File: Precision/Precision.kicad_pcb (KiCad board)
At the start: 2 copper layers, 152 parts, among them J1 M04PTH, J2 M04PTH, J3 M06SIP, J4 M04PTH, J405 Conn_01x08, J406 Conn_01x08, J5 M06SIP, J6 M02PTH, U401 ATMEGA328P-AU, U501 FT232RL, U602 ZF7, Y401 16MHz

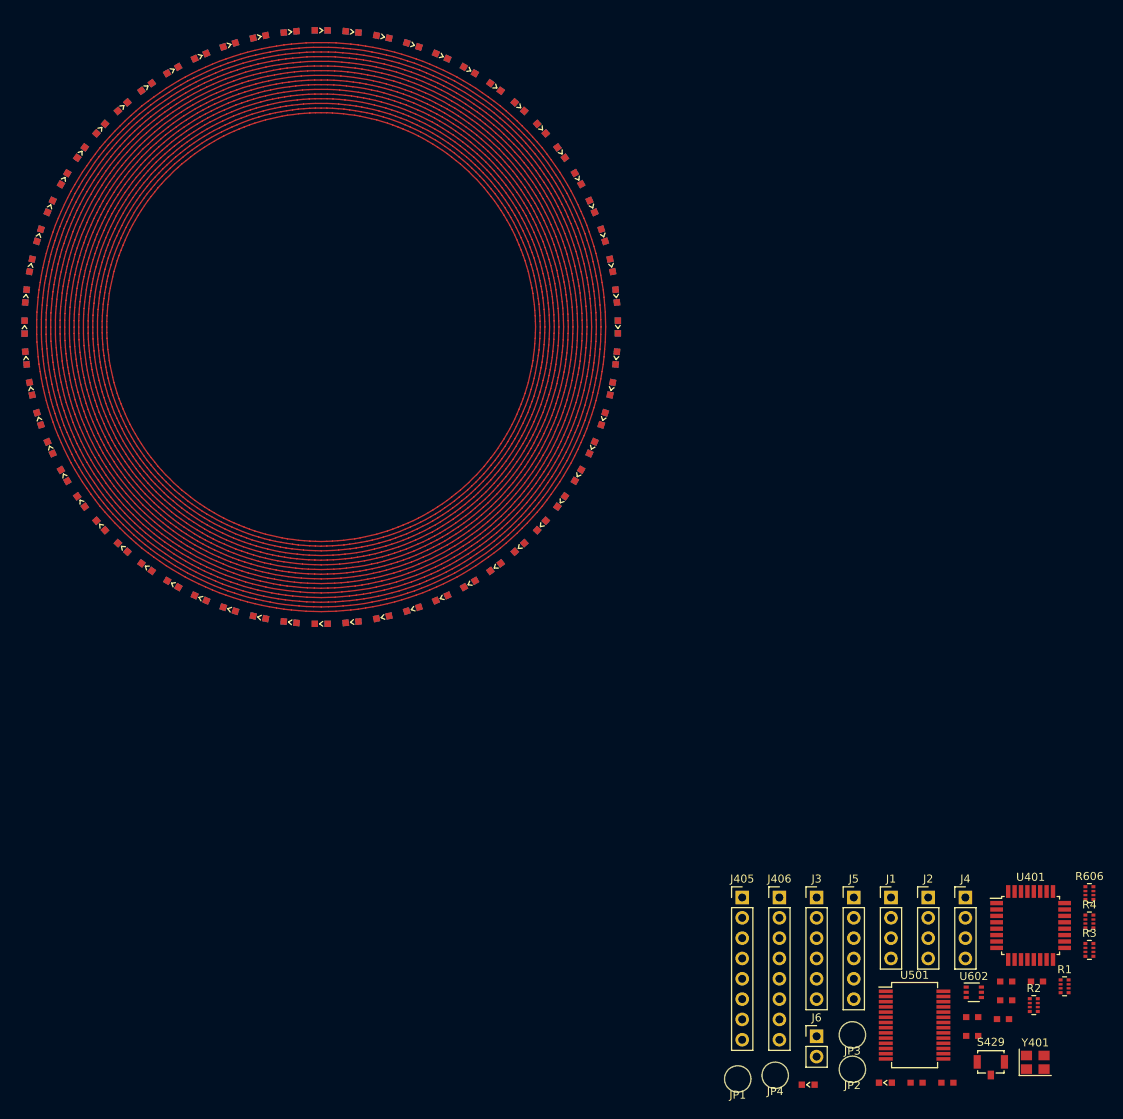
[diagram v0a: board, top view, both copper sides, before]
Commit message: Added Charlieplex traces. The bulk was done with CharlieplexTraces.py, with quite a bit of hand-optimization afterwards
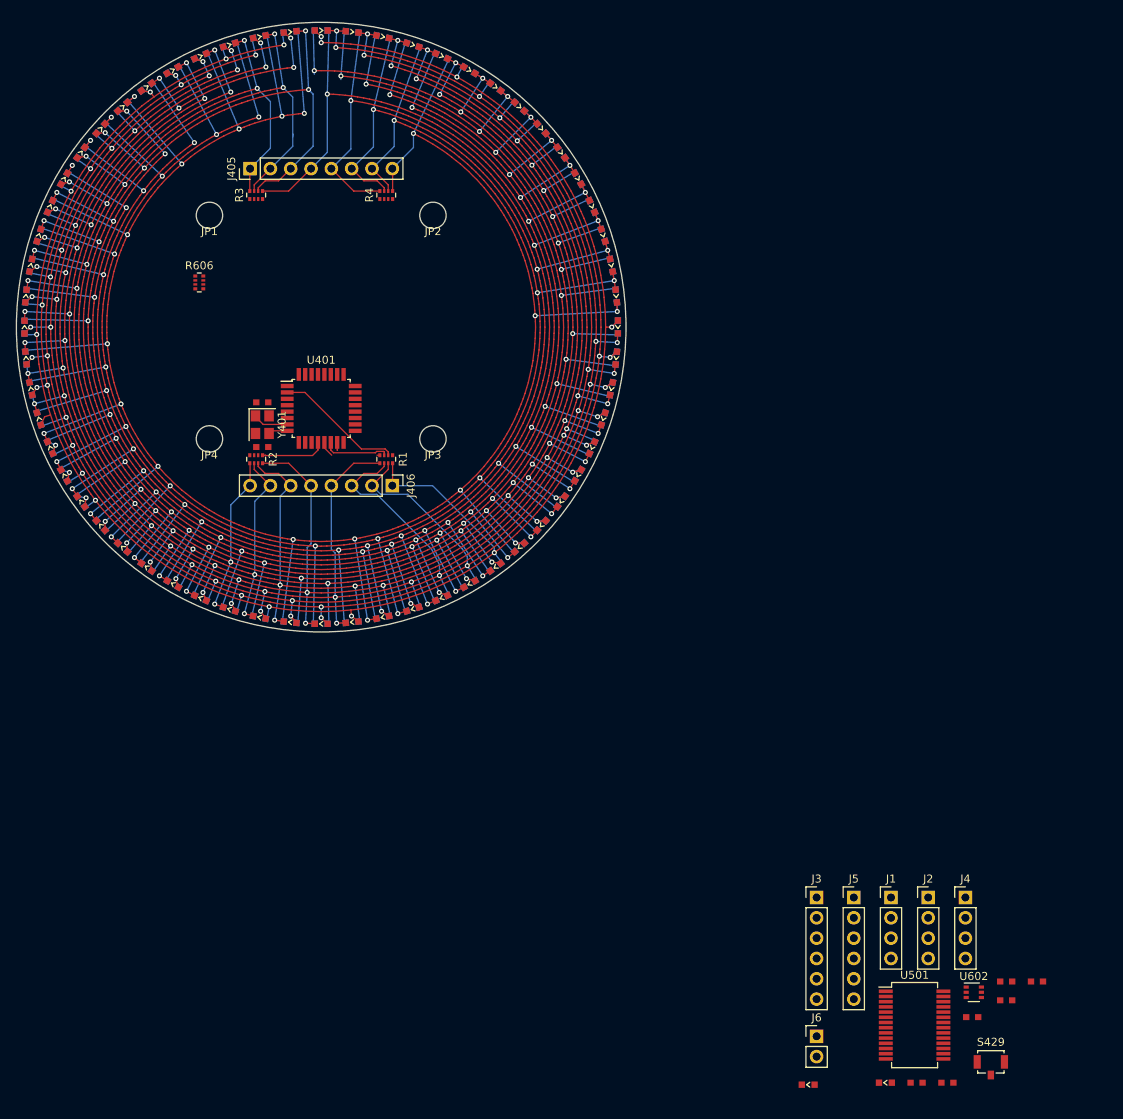
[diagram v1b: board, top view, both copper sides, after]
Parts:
- moved R3 140.5 mm to (42.7, 34.3), turned to 90 degrees
- moved R606 134.9 mm to (35.6, 45.2)
- moved JP1 126.5 mm to (36.8, 36.8)
- moved R4 126.4 mm to (58.9, 34.3), turned to 90 degrees
- moved Y401 125.3 mm to (43.4, 63.0), turned to 270 degrees
- moved C407 120.5 mm to (43.4, 60.2), turned to 180 degrees
- moved JP2 118.9 mm to (64.8, 36.8)
- moved R2 118.8 mm to (42.7, 67.3), turned to 270 degrees
- moved C408 115.3 mm to (43.4, 65.8)
- moved J405 109.9 mm to (41.9, 31.0), turned to 90 degrees
- moved U401 109.7 mm to (50.8, 61.0)
- moved R1 107.4 mm to (58.9, 67.3), turned to 270 degrees
- moved JP4 106.4 mm to (36.8, 64.8)
- moved JP3 91.1 mm to (64.8, 64.8)
- moved J406 70.7 mm to (59.7, 70.6), turned to 270 degrees
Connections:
- D000 pad 1: /Q01 -> /Q02
- D000 pad 2: /Q02 -> /Q01
- D001 pad 1: /Q02 -> /Q03
- D001 pad 2: /Q03 -> /Q02
- D002 pad 1: /Q03 -> /Q04
- D002 pad 2: /Q04 -> /Q03
- D003 pad 1: /Q04 -> /Q05
- D003 pad 2: /Q05 -> /Q04
- D004 pad 1: /Q05 -> /Q06
- D004 pad 2: /Q06 -> /Q05
- D005 pad 1: /Q06 -> /Q07
- D005 pad 2: /Q07 -> /Q06
- D006 pad 1: /Q07 -> /Q08
- D006 pad 2: /Q08 -> /Q07
- D007 pad 1: /Q08 -> /Q09
- D007 pad 2: /Q09 -> /Q08
- D008 pad 1: /Q09 -> /Q10
- D008 pad 2: /Q10 -> /Q09
- D009 pad 1: /Q10 -> /Q11
- D009 pad 2: /Q11 -> /Q10
- D010 pad 1: /Q11 -> /Q12
- D010 pad 2: /Q12 -> /Q11
- D011 pad 1: /Q12 -> /Q13
- D011 pad 2: /Q13 -> /Q12
- D012 pad 1: /Q13 -> /Q14
- D012 pad 2: /Q14 -> /Q13
- D013 pad 1: /Q14 -> /Q15
- D013 pad 2: /Q15 -> /Q14
- D014 pad 1: /Q15 -> /Q16
- D014 pad 2: /Q16 -> /Q15
- D015 pad 1: /Q01 -> /Q03
- D015 pad 2: /Q03 -> /Q01
- D016 pad 1: /Q02 -> /Q04
- D016 pad 2: /Q04 -> /Q02
- D017 pad 1: /Q03 -> /Q05
- D017 pad 2: /Q05 -> /Q03
- D018 pad 1: /Q04 -> /Q06
- D018 pad 2: /Q06 -> /Q04
- D019 pad 1: /Q05 -> /Q07
- D019 pad 2: /Q07 -> /Q05
- D020 pad 1: /Q06 -> /Q08
- D020 pad 2: /Q08 -> /Q06
- D021 pad 1: /Q07 -> /Q09
- D021 pad 2: /Q09 -> /Q07
- D022 pad 1: /Q08 -> /Q10
- D022 pad 2: /Q10 -> /Q08
- D023 pad 1: /Q09 -> /Q11
- D023 pad 2: /Q11 -> /Q09
- D024 pad 1: /Q10 -> /Q12
- D024 pad 2: /Q12 -> /Q10
- D025 pad 1: /Q11 -> /Q13
- D025 pad 2: /Q13 -> /Q11
- D026 pad 1: /Q12 -> /Q14
- D026 pad 2: /Q14 -> /Q12
- D027 pad 1: /Q13 -> /Q15
- D027 pad 2: /Q15 -> /Q13
- D028 pad 1: /Q14 -> /Q16
- D028 pad 2: /Q16 -> /Q14
- D029 pad 1: /Q01 -> /Q04
- D029 pad 2: /Q04 -> /Q01
- D030 pad 1: /Q02 -> /Q05
- D030 pad 2: /Q05 -> /Q02
- D031 pad 1: /Q03 -> /Q06
- D031 pad 2: /Q06 -> /Q03
- D032 pad 1: /Q04 -> /Q07
- D032 pad 2: /Q07 -> /Q04
- D033 pad 1: /Q05 -> /Q08
- D033 pad 2: /Q08 -> /Q05
- D034 pad 1: /Q06 -> /Q09
- D034 pad 2: /Q09 -> /Q06
- D035 pad 1: /Q07 -> /Q10
- D035 pad 2: /Q10 -> /Q07
- D036 pad 1: /Q08 -> /Q11
- D036 pad 2: /Q11 -> /Q08
- D037 pad 1: /Q09 -> /Q12
- D037 pad 2: /Q12 -> /Q09
- D038 pad 1: /Q10 -> /Q13
- D038 pad 2: /Q13 -> /Q10
- D039 pad 1: /Q11 -> /Q14
- D039 pad 2: /Q14 -> /Q11
- D040 pad 1: /Q12 -> /Q15
- D040 pad 2: /Q15 -> /Q12
- D041 pad 1: /Q13 -> /Q16
- D041 pad 2: /Q16 -> /Q13
- D042 pad 1: /Q01 -> /Q05
- D042 pad 2: /Q05 -> /Q01
- D043 pad 1: /Q02 -> /Q06
- D043 pad 2: /Q06 -> /Q02
- D044 pad 1: /Q03 -> /Q07
- D044 pad 2: /Q07 -> /Q03
- D045 pad 1: /Q06 -> /Q08
- D045 pad 2: /Q08 -> /Q04
- D046 pad 1: /Q05 -> /Q09
- D046 pad 2: /Q09 -> /Q05
- D047 pad 1: /Q06 -> /Q10
- D047 pad 2: /Q10 -> /Q06
- D048 pad 1: /Q07 -> /Q11
- D048 pad 2: /Q11 -> /Q07
- D049 pad 1: /Q08 -> /Q12
- D049 pad 2: /Q12 -> /Q08
- D050 pad 1: /Q09 -> /Q13
- D050 pad 2: /Q13 -> /Q09
- D051 pad 1: /Q10 -> /Q14
- D051 pad 2: /Q14 -> /Q10
- D052 pad 1: /Q11 -> /Q15
- D052 pad 2: /Q15 -> /Q11
- D053 pad 1: /Q12 -> /Q16
- D053 pad 2: /Q16 -> /Q12
- D054 pad 1: /Q01 -> /Q06
- D054 pad 2: /Q06 -> /Q01
- D055 pad 1: /Q02 -> /Q07
- D055 pad 2: /Q07 -> /Q02
- D056 pad 1: /Q03 -> /Q08
- D056 pad 2: /Q08 -> /Q03
- D057 pad 1: /Q06 -> /Q09
- D057 pad 2: /Q09 -> /Q04
- D058 pad 1: /Q05 -> /Q10
- D058 pad 2: /Q10 -> /Q05
- D059 pad 1: /Q06 -> /Q11
- D059 pad 2: /Q11 -> /Q06
- D100 pad 1: /Q07 -> /Q12
- D100 pad 2: /Q12 -> /Q07
- D101 pad 1: /Q08 -> /Q13
- D101 pad 2: /Q13 -> /Q08
- D102 pad 1: /Q09 -> /Q14
- D102 pad 2: /Q14 -> /Q09
- D103 pad 1: /Q10 -> /Q15
- D103 pad 2: /Q15 -> /Q10
- D104 pad 1: /Q11 -> /Q16
- D104 pad 2: /Q16 -> /Q11
- D105 pad 1: /Q01 -> /Q07
- D105 pad 2: /Q07 -> /Q01
- D106 pad 1: /Q02 -> /Q08
- D106 pad 2: /Q08 -> /Q02
- D107 pad 1: /Q03 -> /Q09
- D107 pad 2: /Q09 -> /Q03
- D108 pad 1: /Q06 -> /Q10
- D108 pad 2: /Q10 -> /Q04
- D109 pad 1: /Q05 -> /Q11
- D109 pad 2: /Q11 -> /Q05
- D110 pad 1: /Q06 -> /Q12
- D110 pad 2: /Q12 -> /Q06
- D111 pad 1: /Q07 -> /Q13
- D111 pad 2: /Q13 -> /Q07
- D112 pad 1: /Q08 -> /Q14
- D112 pad 2: /Q14 -> /Q08
- D113 pad 1: /Q09 -> /Q15
- D113 pad 2: /Q15 -> /Q09
- D114 pad 1: /Q10 -> /Q16
- D114 pad 2: /Q16 -> /Q10
- D115 pad 1: /Q01 -> /Q08
- D115 pad 2: /Q08 -> /Q01
- D116 pad 1: /Q02 -> /Q09
- D116 pad 2: /Q09 -> /Q02
- D117 pad 1: /Q03 -> /Q10
- D117 pad 2: /Q10 -> /Q03
- D118 pad 1: /Q06 -> /Q11
- D118 pad 2: /Q11 -> /Q04
- D119 pad 1: /Q05 -> /Q12
- D119 pad 2: /Q12 -> /Q05
- D120 pad 1: /Q06 -> /Q13
- D120 pad 2: /Q13 -> /Q06
- D121 pad 1: /Q07 -> /Q14
- D121 pad 2: /Q14 -> /Q07
- D122 pad 1: /Q08 -> /Q15
- D122 pad 2: /Q15 -> /Q08
- D123 pad 1: /Q09 -> /Q16
- D123 pad 2: /Q16 -> /Q09
- D124 pad 1: /Q01 -> /Q09
- D124 pad 2: /Q09 -> /Q01
- D125 pad 1: /Q02 -> /Q10
- D125 pad 2: /Q10 -> /Q02
- D126 pad 1: /Q03 -> /Q11
- D126 pad 2: /Q11 -> /Q03
- D127 pad 1: /Q06 -> /Q12
- D127 pad 2: /Q12 -> /Q04
- D128 pad 1: /Q05 -> /Q13
- D128 pad 2: /Q13 -> /Q05
- D129 pad 1: /Q06 -> /Q14
- D129 pad 2: /Q14 -> /Q06
- D130 pad 1: /Q07 -> /Q15
- D130 pad 2: /Q15 -> /Q07
- D131 pad 1: /Q08 -> /Q16
- D131 pad 2: /Q16 -> /Q08
- D132 pad 1: /Q01 -> /Q10
- D132 pad 2: /Q10 -> /Q01
- D133 pad 1: /Q02 -> /Q11
- D133 pad 2: /Q11 -> /Q02
- D134 pad 1: /Q03 -> /Q12
- D134 pad 2: /Q12 -> /Q03
- D135 pad 1: /Q06 -> /Q13
- D135 pad 2: /Q13 -> /Q04
- D136 pad 1: /Q05 -> /Q14
- D136 pad 2: /Q14 -> /Q05
- D137 pad 1: /Q06 -> /Q15
- D137 pad 2: /Q15 -> /Q06
- D138 pad 1: /Q07 -> /Q16
- D138 pad 2: /Q16 -> /Q07
- D139 pad 1: /Q01 -> /Q11
- D139 pad 2: /Q11 -> /Q01
- D140 pad 1: /Q02 -> /Q12
- D140 pad 2: /Q12 -> /Q02
- D141 pad 1: /Q03 -> /Q13
- D141 pad 2: /Q13 -> /Q03
- D142 pad 1: /Q06 -> /Q14
- D142 pad 2: /Q14 -> /Q04
- D143 pad 1: /Q05 -> /Q15
- D143 pad 2: /Q15 -> /Q05
- D144 pad 1: /Q06 -> /Q16
- D144 pad 2: /Q16 -> /Q06
- D145 pad 1: /Q01 -> /Q12
- D145 pad 2: /Q12 -> /Q01
- D146 pad 1: /Q02 -> /Q13
- D146 pad 2: /Q13 -> /Q02
- D147 pad 1: /Q03 -> /Q14
- D147 pad 2: /Q14 -> /Q03
- D148 pad 1: /Q06 -> /Q15
- D148 pad 2: /Q15 -> /Q04
- D149 pad 1: /Q05 -> /Q16
- D149 pad 2: /Q16 -> /Q05
- D150 pad 1: /Q01 -> /Q13
- D150 pad 2: /Q13 -> /Q01
- D151 pad 1: /Q02 -> /Q14
- D151 pad 2: /Q14 -> /Q02
- D152 pad 1: /Q03 -> /Q15
- D152 pad 2: /Q15 -> /Q03
- D153 pad 1: /Q06 -> /Q16
- D153 pad 2: /Q16 -> /Q04
- D154 pad 1: /Q01 -> /Q14
- D154 pad 2: /Q14 -> /Q01
- D155 pad 1: /Q02 -> /Q15
- D155 pad 2: /Q15 -> /Q02
- D156 pad 1: /Q03 -> /Q16
- D156 pad 2: /Q16 -> /Q03
- D157 pad 1: /Q01 -> /Q15
- D157 pad 2: /Q15 -> /Q01
- D158 pad 1: /Q02 -> /Q16
- D158 pad 2: /Q16 -> /Q02
- D159 pad 1: /Q01 -> /Q16
- D159 pad 2: /Q16 -> /Q01
- J405 pad 1: /Q01 -> /Q09
- J405 pad 2: /Q02 -> /Q10
- J405 pad 3: /Q03 -> /Q11
- J405 pad 4: /Q04 -> /Q12
- J405 pad 5: /Q05 -> /Q13
- J405 pad 6: /Q06 -> /Q14
- J405 pad 7: /Q07 -> /Q15
- J405 pad 8: /Q08 -> /Q16
- J406 pad 1: /Q09 -> /Q01
- J406 pad 2: /Q10 -> /Q02
- J406 pad 3: /Q11 -> /Q03
- J406 pad 4: /Q12 -> /Q04
- J406 pad 5: /Q13 -> /Q05
- J406 pad 6: /Q14 -> /Q06
- J406 pad 7: /Q15 -> /Q07
- J406 pad 8: /Q16 -> /Q08
- U401 pad 19: Net-(U401-Pad19) -> (no net)
- U401 pad 22: Net-(U401-Pad22) -> (no net)
- U501 pad 10: Net-(U501-Pad10) -> (no net)
- U501 pad 11: Net-(U501-Pad11) -> (no net)
- U501 pad 12: Net-(U501-Pad12) -> (no net)
- U501 pad 13: Net-(U501-Pad13) -> (no net)
- U501 pad 14: Net-(U501-Pad14) -> (no net)
- U501 pad 19: Net-(U501-Pad19) -> (no net)
- U501 pad 27: Net-(U501-Pad27) -> (no net)
- U501 pad 28: Net-(U501-Pad28) -> (no net)
- U501 pad 3: Net-(U501-Pad3) -> (no net)
- U501 pad 6: Net-(U501-Pad6) -> (no net)
- U501 pad 9: Net-(U501-Pad9) -> (no net)
- Y401 pad 2: Net-(Y401-Pad2) -> (no net)
- Y401 pad 4: Net-(Y401-Pad4) -> (no net)
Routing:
- net /Q16: track 168.4 -> 302.6 mm, vias 0 -> 17
- net /Q15: track 172.0 -> 289.5 mm, vias 0 -> 16
- net /Q14: track 175.7 -> 283.3 mm, vias 0 -> 17
- net /Q11: track 186.7 -> 288.6 mm, vias 0 -> 20
- net /Q12: track 183.0 -> 282.7 mm, vias 0 -> 19
- net /Q10: track 190.4 -> 288.9 mm, vias 0 -> 21
- net /Q13: track 179.4 -> 265.7 mm, vias 0 -> 17
- net /Q09: track 194.1 -> 278.5 mm, vias 0 -> 20
- net /Q08: track 197.7 -> 274.1 mm, vias 0 -> 20
- net /Q07: track 201.4 -> 272.7 mm, vias 0 -> 20
- net /Q06: track 205.1 -> 267.6 mm, vias 0 -> 21
- net /Q05: track 208.7 -> 268.0 mm, vias 0 -> 21
- net /Q04: track 212.4 -> 263.4 mm, vias 0 -> 20
- net /Q03: track 216.1 -> 257.4 mm, vias 0 -> 18
- net /Q02: track 219.8 -> 261.0 mm, vias 0 -> 17
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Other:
- board outline added: 76.2 x 76.2 mm
- net class Default: clearance 0.2 -> 0.1524; trace_width 0.25 -> 0.1524; via_dia 0.8 -> 0.635; via_drill 0.4 -> 0.3302
- rule trace_clearance: 0.2 -> 0.1524

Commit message: Finished connecting all signals, added buttons for setting time
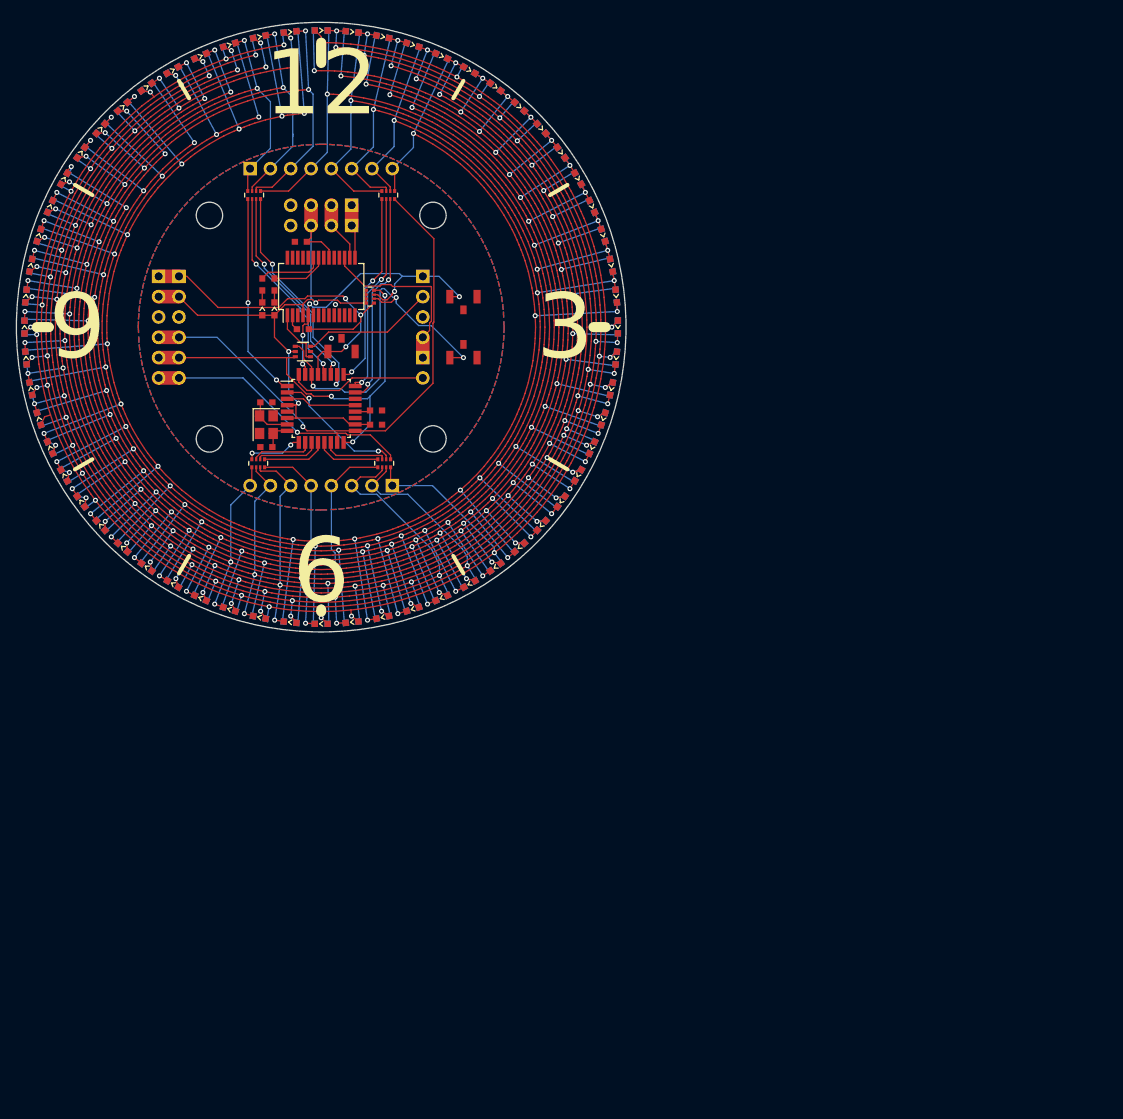
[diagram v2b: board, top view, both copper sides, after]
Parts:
- added REF**: KiCAD Logo, KwanSystems:Symbol_KiCAD-Logo_CopperAndSilkScreenTop_small, B.Cu at (24.6, 51.6)
- added REF**: OSHW-Symbol_6.7x6mm_SilkScreen, Symbol:OSHW-Symbol_6.7x6mm_SilkScreen, B.Cu at (24.9, 45.5)
- added REF**: StKwans, KwanSystems:ADivisionOf, B.Cu at (37.3, 24.4)
- added REF**: StKwans, KwanSystems:StKwans, B.Cu at (56.6, 20.8)
- added REF**: PrecisionKwan, KwanSystems:PrecisionKwan, B.Cu at (50.8, 50.8)
- added S430: B3U-1100P, KwanSystems:SW_SPST_B3U-1100P, F.Cu at (68.6, 54.6)
- added S431: B3U-1100P, KwanSystems:SW_SPST_B3U-1100P, F.Cu at (68.6, 47.0)
- J1, J2, J3, J4, J405, J406, J5, J6: moved to B.Cu
- S429: footprint Button_Switch_SMD:SW_SPST_B3U-1100P -> KwanSystems:SW_SPST_B3U-1100P
- moved R501 131.5 mm to (43.4, 45.5), turned to 270 degrees
- moved C10 129.5 mm to (48.3, 40.1), turned to 180 degrees
- moved R502 129.1 mm to (45.0, 45.5), turned to 270 degrees
- moved D501 124.2 mm to (43.4, 48.5), turned to 270 degrees
- moved S429 120.9 mm to (53.3, 53.8), turned to 180 degrees
- moved C502 120.0 mm to (48.5, 51.1), turned to 180 degrees
- moved U501 118.4 mm to (50.8, 45.7), turned to 90 degrees
- moved D502 117.7 mm to (45.0, 48.5), turned to 270 degrees
- moved J5 116.5 mm to (30.5, 44.5), turned to 180 degrees
- moved U602 116.0 mm to (48.5, 53.8), turned to 180 degrees
- moved J2 112.6 mm to (54.6, 35.6), turned to 90 degrees
- moved J3 111.3 mm to (33.0, 44.5), turned to 180 degrees
- moved J1 107.7 mm to (54.6, 38.1), turned to 90 degrees
- moved C418 106.4 mm to (57.7, 63.0), turned to 180 degrees
- moved C420 106.3 mm to (57.7, 61.2)
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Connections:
- net Net-(C420-Pad1) renamed /AREF
- net Net-(C502-Pad2) renamed /DTR
- net Net-(D501-Pad1) renamed /TXLED+
- net Net-(D502-Pad1) renamed /RXLED+
- net Net-(R501-Pad1) renamed /TXLED-
- net Net-(R502-Pad1) renamed /RXLED-
- R606 pad 2: (no net) -> +5V
- R606 pad 3: (no net) -> +5V
- R606 pad 6: (no net) -> /AT_RX
- R606 pad 7: (no net) -> /AT_TX
- S429 pad 1: /RESET -> GND
- S429 pad 2: GND -> /RESET
- Y401 pad 2: (no net) -> GND
- Y401 pad 4: (no net) -> GND
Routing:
- net +5V: track 0.00 -> 79.0 mm, vias 0 -> 3
- net /P16: track 0.00 -> 67.0 mm, vias 0 -> 1
- net /D12: track 0.00 -> 53.8 mm, vias 0 -> 3
- net /RESET: track 0.00 -> 49.5 mm, vias 0 -> 3
- net /AT_RX: track 0.00 -> 45.9 mm, vias 0 -> 3
- net /AT_TX: track 0.00 -> 38.2 mm, vias 0 -> 5
- net /P01: track 1.00 -> 34.7 mm, vias 0 -> 1
- net /P12: track 0.00 -> 28.6 mm, vias 0 -> 2
- net /P15: track 0.00 -> 26.8 mm, vias 0 -> 2
- net /P11: track 0.00 -> 26.0 mm, vias 0 -> 2
- net /P09: track 0.00 -> 25.8 mm, vias 0 -> 2
- net /P10: track 0.00 -> 25.7 mm, vias 0 -> 2
- net /P14: track 0.00 -> 25.4 mm, vias 0 -> 2
- net /P13: track 0.00 -> 24.3 mm, vias 0 -> 2
- net +3V3: track 0.00 -> 22.4 mm
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- added copper zone on B.Cu, net GND
- added copper zone on F.Cu, net GND
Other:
- board text added: "12"
- board text added: "25 Dec 2019"
- board text added: "3"
- board text added: "5V"
- board text added: "6"
- board text added: "9"
- board text added: "D+"
- board text added: "D-"
- board text added: "Designed using"
- board text added: "GND"
- board text added: "Project Precision"
- board text added: "black"
- board text added: "green"
- board text added: "red"
- board text added: "version 2.0"
- board text added: "white"

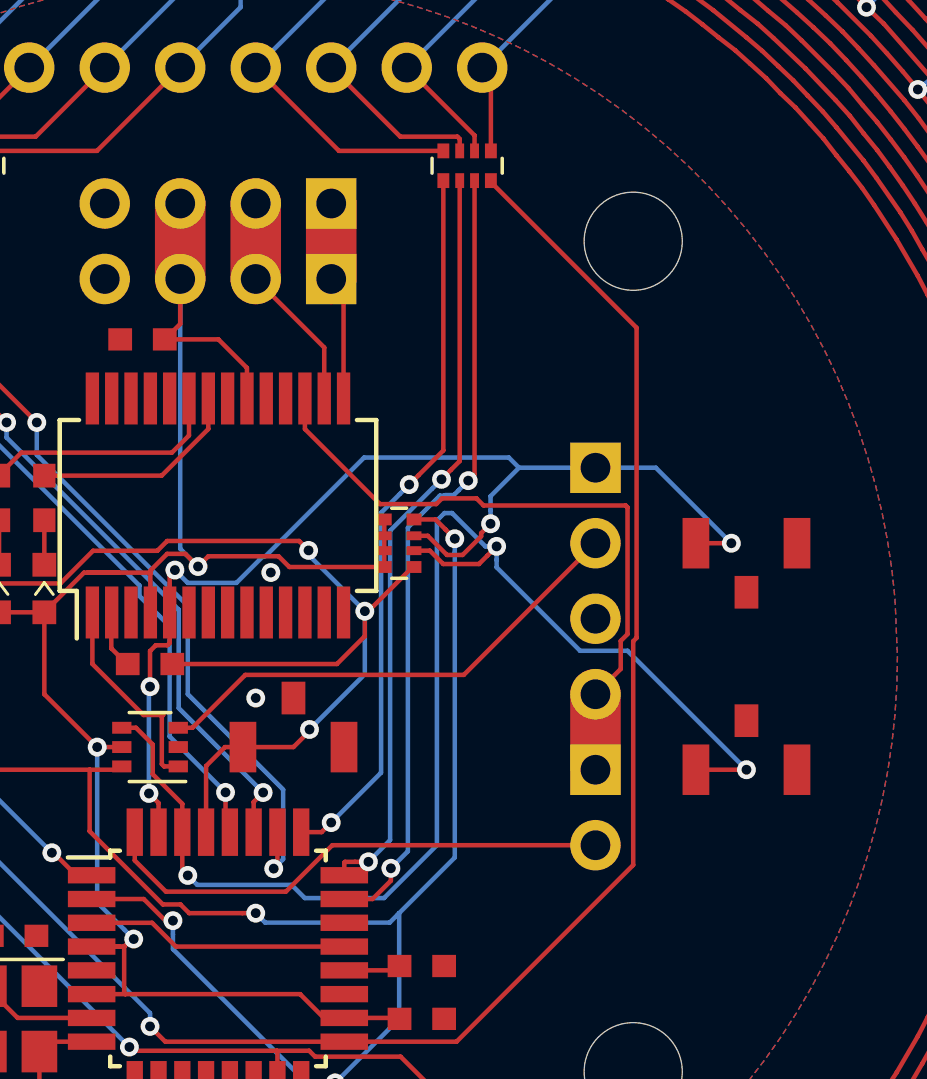
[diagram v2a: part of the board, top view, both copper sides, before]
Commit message: Moved manual set buttons to the GPS TX/RX lines
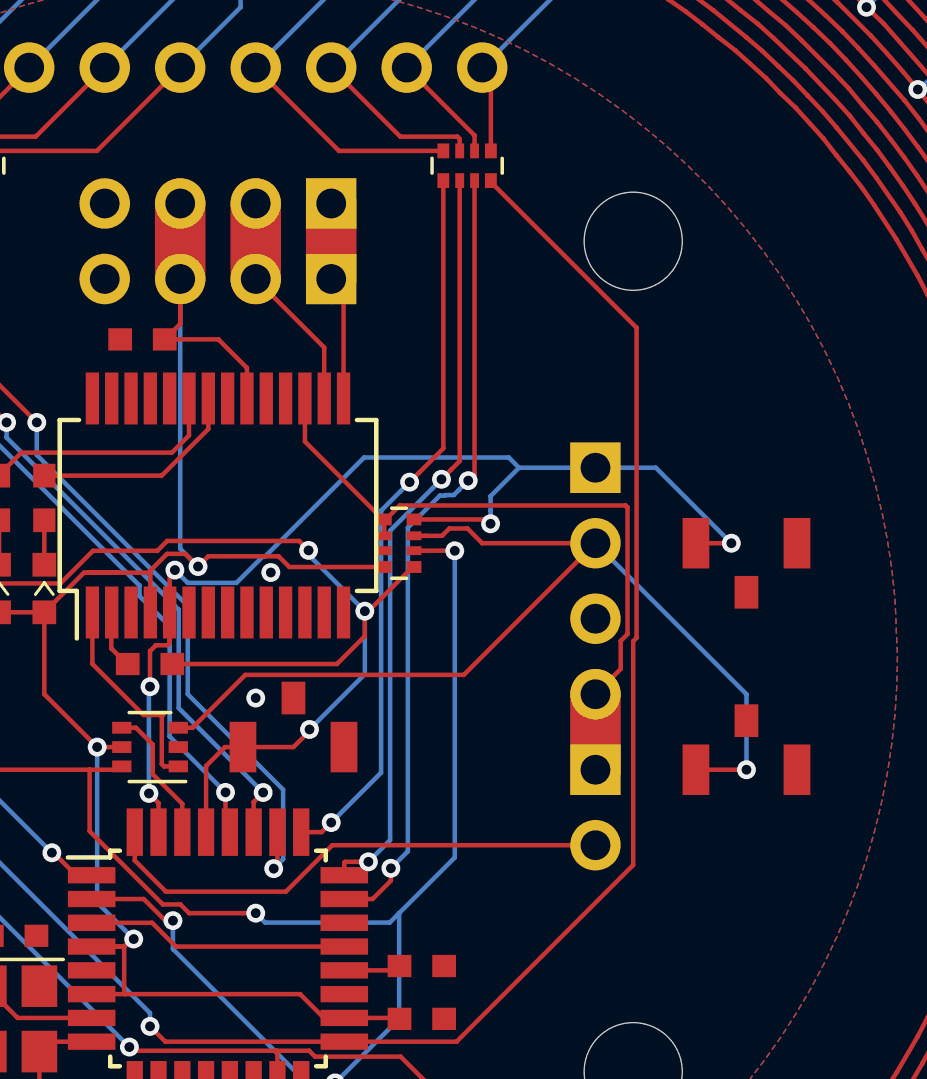
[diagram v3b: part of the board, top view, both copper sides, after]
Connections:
- R606 pad 1: +5V -> +3V3
- R606 pad 2: +5V -> +3V3
- R606 pad 6: /AT_RX -> /D12
- R606 pad 7: /AT_TX -> /GPS_TX
- R606 pad 8: /D12 -> /AT_TX
- S430 pad 2: /AT_RX -> /GPS_TX
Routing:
- net /AT_RX: track 45.9 -> 4.63 mm, vias 3 -> 0
- net /GPS_TX: track 16.6 -> 34.4 mm, vias 0 -> 1
- net +5V: track 79.0 -> 77.4 mm
- net +3V3: track 22.4 -> 23.5 mm
- net /D12: track 53.8 -> 53.1 mm
- net /AT_TX: track 38.2 -> 37.5 mm
